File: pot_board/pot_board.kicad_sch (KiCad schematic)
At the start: 3 parts, among them J1 Conn_01x06

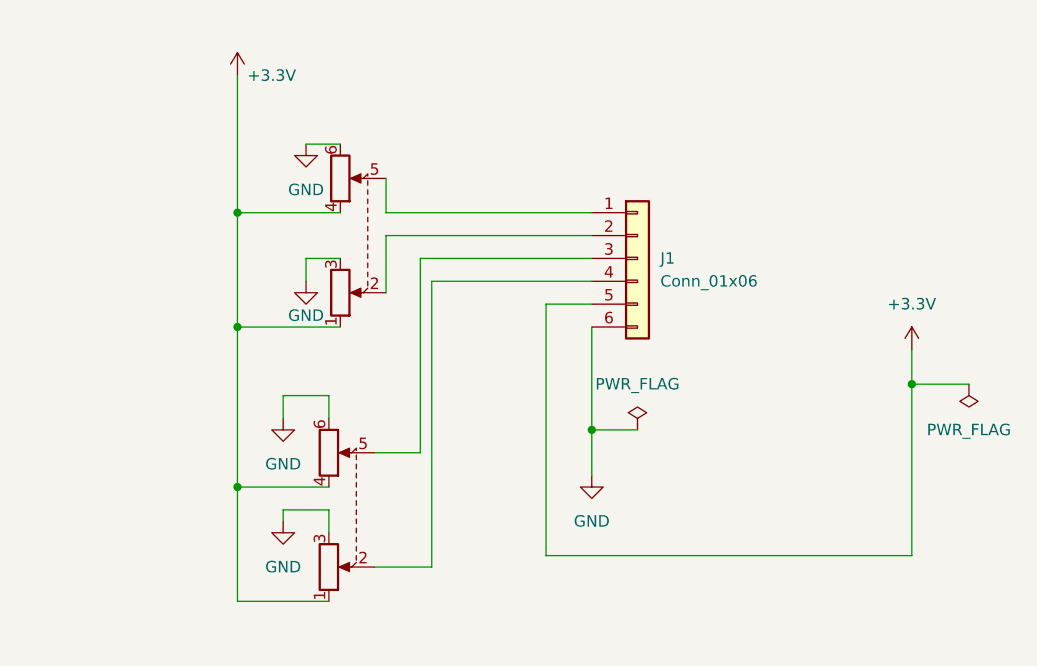
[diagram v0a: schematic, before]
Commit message: update main board routing, add 3d models and improve layout
Changes:

* update main board layout a bit
* try to improve routing
* add 3d model for 6p6c
* add decoupling caps to ptt line
* almost finish pot board
* switch board almost finished

Details:
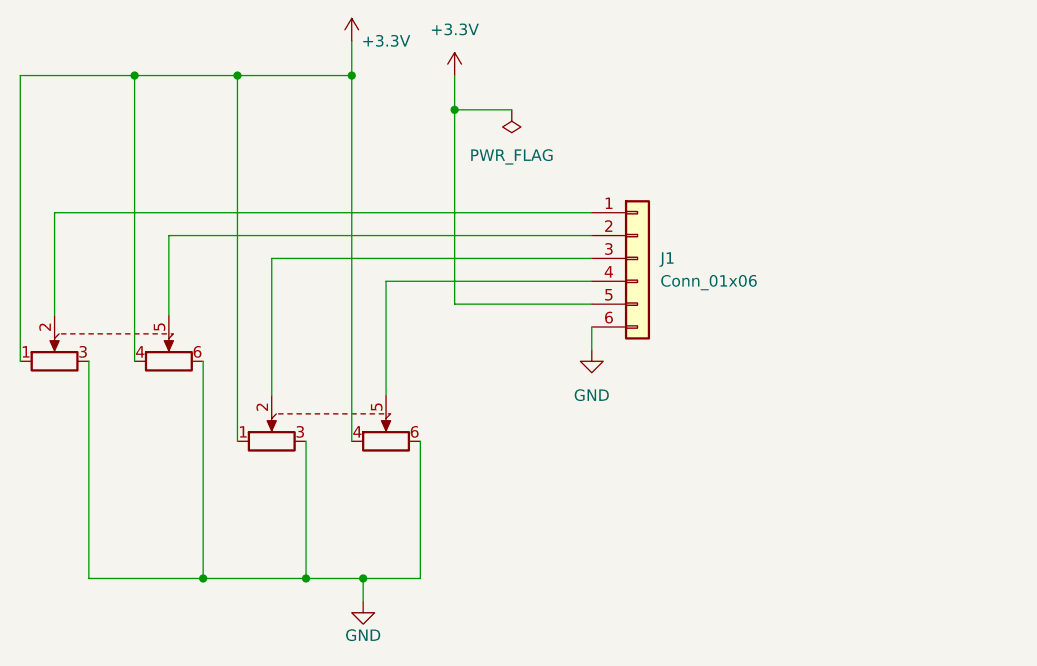
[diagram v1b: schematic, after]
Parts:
- J1: footprint Connector_IDC:IDC-Header_2x03_P2.54mm_Horizontal -> Connector_JST:JST_XH_B6B-XH-A_1x06_P2.50mm_Vertical
- RV1, RV2: footprint Potentiometer_THT:Potentiometer_Alps_RK097_Dual_Horizontal_Switch -> CustomLibrary:Potentiometer_Alps_RK097_Dual_Horizontal
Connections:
- net at RV1.2: now also J1.1 (Pin_1); no longer J1.2 (Pin_2)
- net at RV1.5: now also J1.2 (Pin_2); no longer J1.1 (Pin_1)
- net at RV2.2: now also J1.3 (Pin_3); no longer J1.4 (Pin_4)
- net at RV2.5: now also J1.4 (Pin_4); no longer J1.3 (Pin_3)
